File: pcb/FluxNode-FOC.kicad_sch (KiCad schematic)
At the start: 0 parts

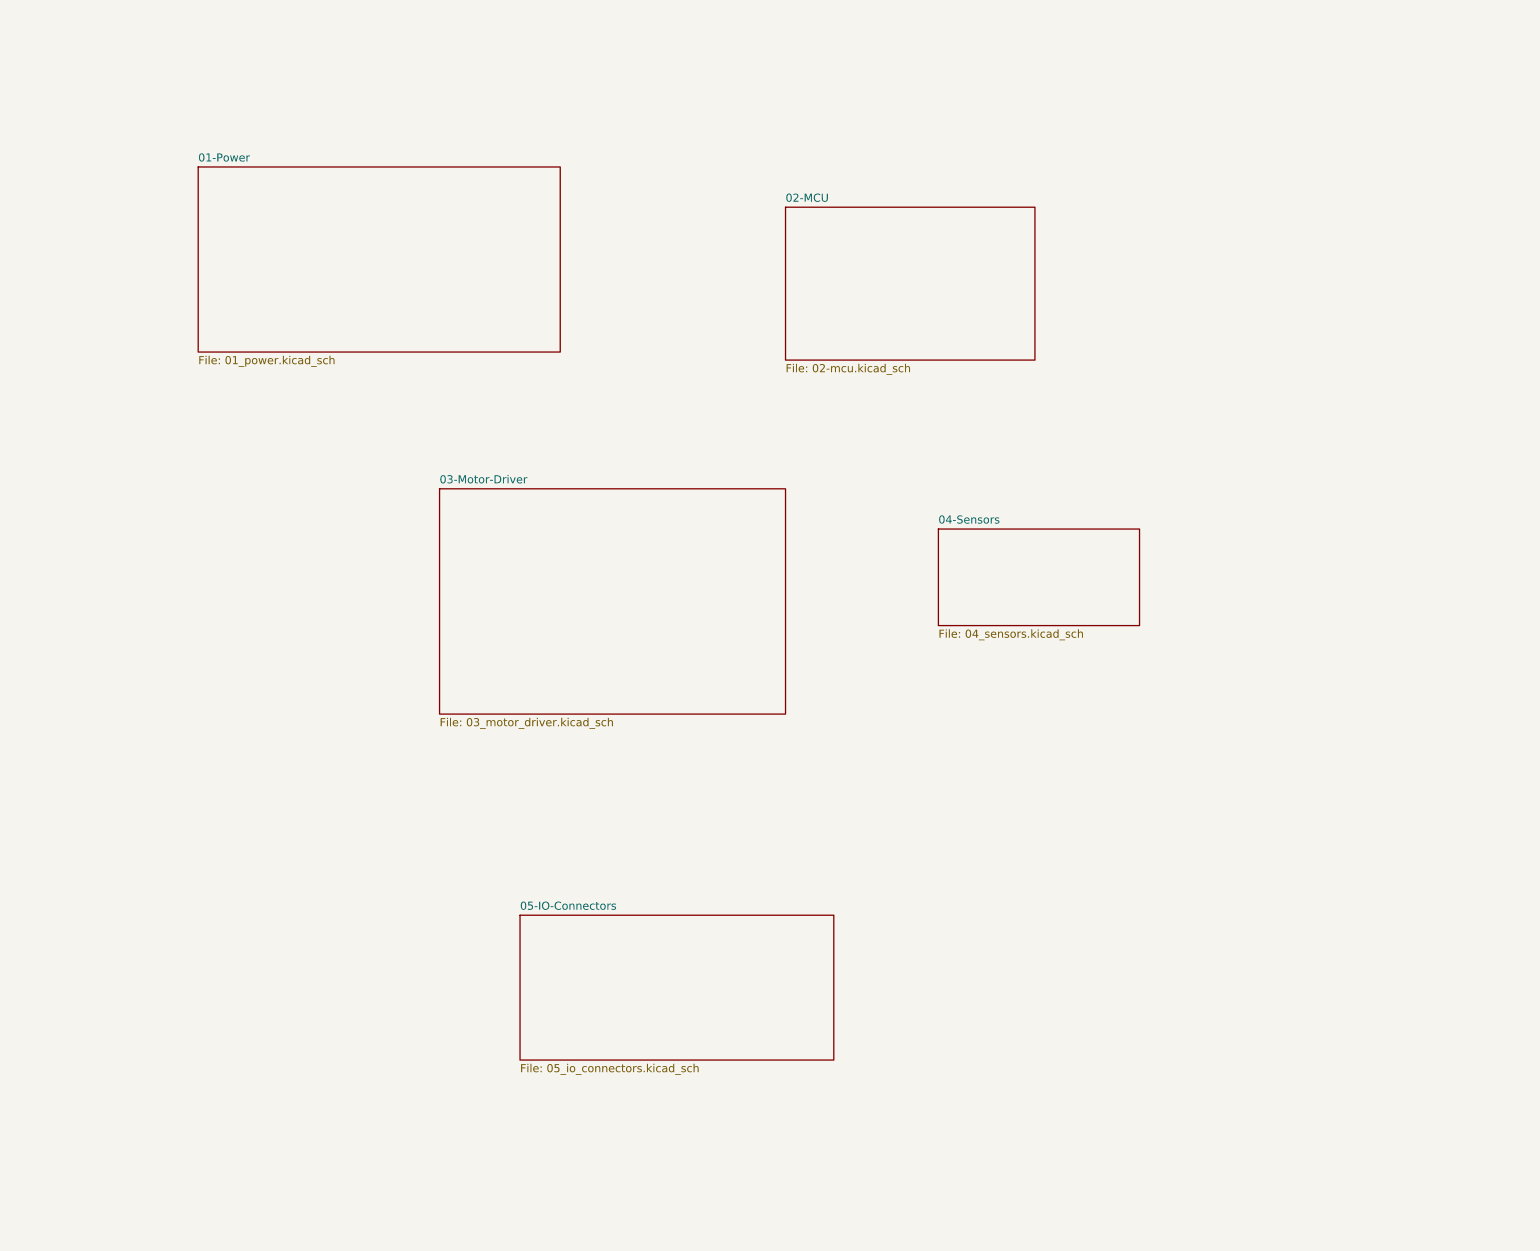
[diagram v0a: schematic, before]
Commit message: Setup project structure with organised sub-sheets
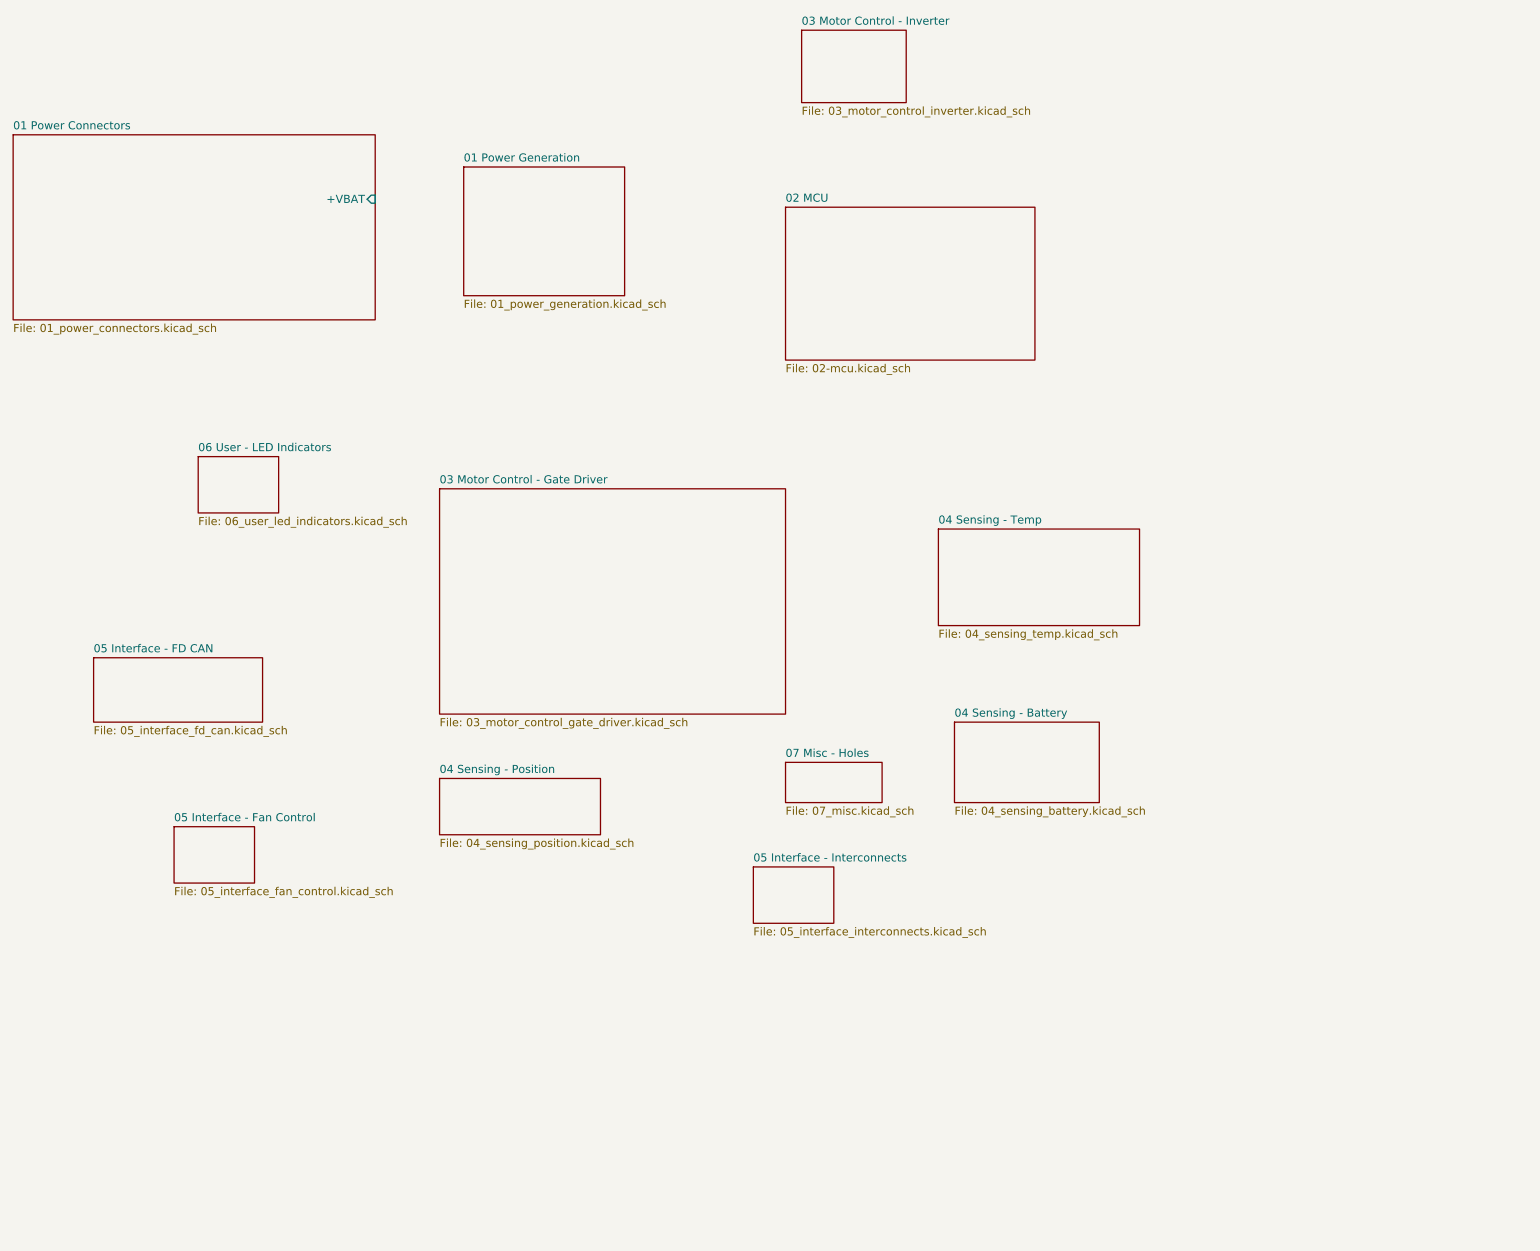
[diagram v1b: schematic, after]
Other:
- sheet 01-Power renamed 01 Power Connectors
- sheet 02-MCU renamed 02 MCU
- sheet 03-Motor-Driver renamed 03 Motor Control - Gate Driver
- sheet 04-Sensors renamed 04 Sensing - Temp
- removed sheet 05-IO-Connectors
- added sheet 01 Power Generation (01_power_generation.kicad_sch)
- added sheet 03 Motor Control - Inverter (03_motor_control_inverter.kicad_sch)
- added sheet 04 Sensing - Battery (04_sensing_battery.kicad_sch)
- added sheet 04 Sensing - Position (04_sensing_position.kicad_sch)
- added sheet 05 Interface - FD CAN (05_interface_fd_can.kicad_sch)
- added sheet 05 Interface - Fan Control (05_interface_fan_control.kicad_sch)
- added sheet 05 Interface - Interconnects (05_interface_interconnects.kicad_sch)
- added sheet 06 User - LED Indicators (06_user_led_indicators.kicad_sch)
- added sheet 07 Misc - Holes (07_misc.kicad_sch)
- sheet 01 Power Connectors: file 01_power.kicad_sch -> 01_power_connectors.kicad_sch
- sheet 01 Power Connectors ports: added +VBAT; removed none
- sheet 03 Motor Control - Gate Driver: file 03_motor_driver.kicad_sch -> 03_motor_control_gate_driver.kicad_sch
- sheet 04 Sensing - Temp: file 04_sensors.kicad_sch -> 04_sensing_temp.kicad_sch

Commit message: Created blockout and connections of all the major parts
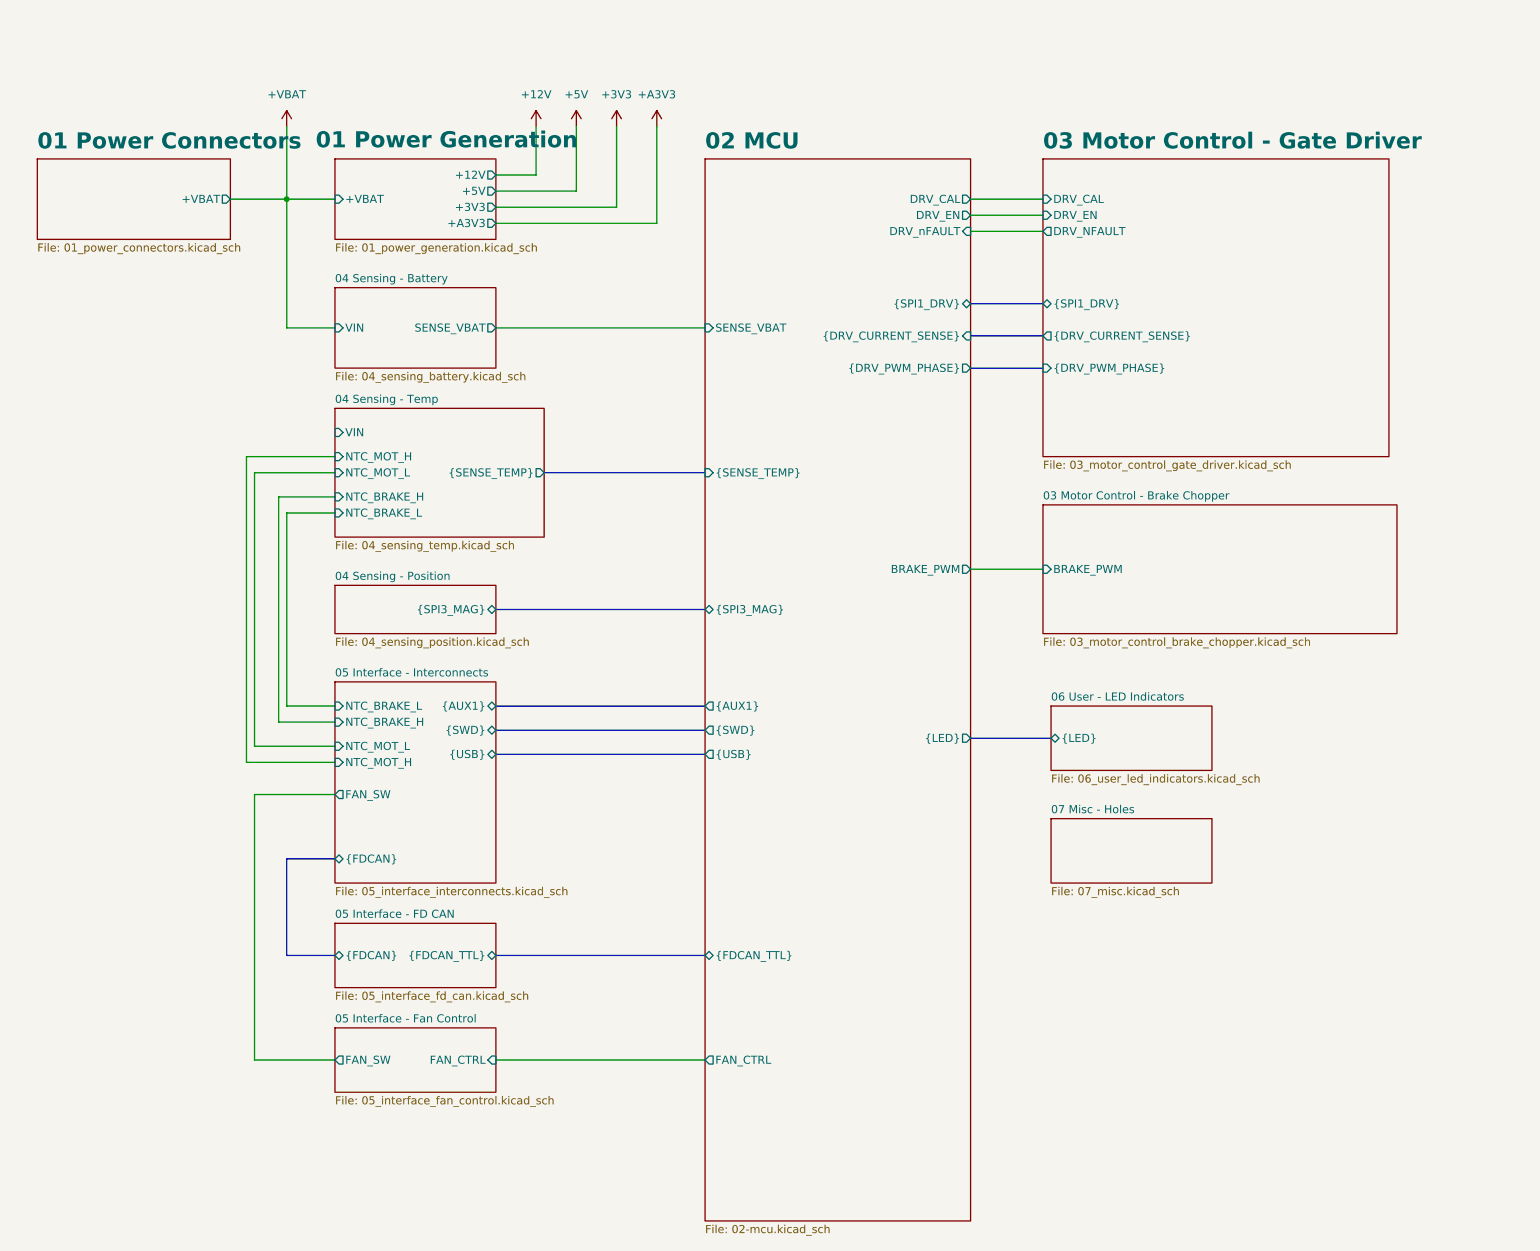
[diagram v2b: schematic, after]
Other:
- removed sheet 03 Motor Control - Inverter
- added sheet 03 Motor Control - Brake Chopper (03_motor_control_brake_chopper.kicad_sch)
- sheet 01 Power Generation ports: added +12V, +3V3, +5V, +A3V3, +VBAT; removed none
- sheet 02 MCU ports: added BRAKE_PWM, DRV_CAL, DRV_EN, DRV_nFAULT, FAN_CTRL, SENSE_VBAT, {AUX1}, {DRV_CURRENT_SENSE}, {DRV_PWM_PHASE}, {FDCAN_TTL}, {LED}, {SENSE_TEMP}, {SPI1_DRV}, {SPI3_MAG}, {SWD}, {USB}; removed none
- sheet 03 Motor Control - Gate Driver ports: added DRV_CAL, DRV_EN, DRV_NFAULT, {DRV_CURRENT_SENSE}, {DRV_PWM_PHASE}, {SPI1_DRV}; removed none
- sheet 04 Sensing - Battery ports: added SENSE_VBAT, VIN; removed none
- sheet 04 Sensing - Position ports: added {SPI3_MAG}; removed none
- sheet 04 Sensing - Temp ports: added NTC_BRAKE_H, NTC_BRAKE_L, NTC_MOT_H, NTC_MOT_L, VIN, {SENSE_TEMP}; removed none
- sheet 05 Interface - FD CAN ports: added {FDCAN_TTL}, {FDCAN}; removed none
- sheet 05 Interface - Fan Control ports: added FAN_CTRL, FAN_SW; removed none
- sheet 05 Interface - Interconnects ports: added FAN_SW, NTC_BRAKE_H, NTC_BRAKE_L, NTC_MOT_H, NTC_MOT_L, {AUX1}, {FDCAN}, {SWD}, {USB}; removed none
- sheet 06 User - LED Indicators ports: added {LED}; removed none

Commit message: Unified all different LCSC part numbers of the same exact components to just one variant
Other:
- sheet 02 MCU ports: added BRAKE_CTRL, {SENSE_PHASE_U}, {SPI1_MAG}; removed BRAKE_PWM, {SPI3_MAG}
- sheet 03 Motor Control - Brake Chopper ports: added BRAKE_CTRL, BRAKE_SW; removed BRAKE_PWM
- sheet 04 Sensing - Position ports: added {SPI1_MAG}; removed {SPI3_MAG}
- sheet 05 Interface - Interconnects ports: added BRAKE_SW; removed none
- company: (none) -> PhiMai
- title: (none) -> Project Blockout
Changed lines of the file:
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@@
 	(generator_version "10.0")
 	(paper "A3")
+	(title_block
+		(title "Project Blockout")
+		(date "2026-06-07")
+		(rev "0.1.0")
+		(company "PhiMai")
+	)
 	(junction
 		(at 64.77 46.99)
@@
 	(wire
 		(pts
+			(xy 58.42 140.97) (xy 72.39 140.97)
+		)
+		(stroke
+			(width 0)
+			(type default)
+		)
+	)
+	(wire
+		(pts
 			(xy 64.77 127) (xy 72.39 127)
 		)
@@
 	(wire
 		(pts
-			(xy 72.39 140.97) (xy 59.69 140.97)
+			(xy 72.39 146.05) (xy 59.69 146.05)
 		)
 		(stroke
@@
 		)
 	)
+	(wire
+		(pts
+			(xy 219.71 105.41) (xy 238.76 105.41)
+		)
+		(stroke
+			(width 0)
+			(type default)
+		)
+	)
 	(bus
 		(pts
@@
 	(wire
 		(pts
-			(xy 59.69 140.97) (xy 59.69 182.88)
+			(xy 59.69 146.05) (xy 59.69 182.88)
 		)
 		(stroke
@@
 			(width 0)
 			(type default)
+		)
+	)
+	(label "BRAKE_SW"
+		(at 238.76 105.41 180)
+		(effects
+			(font
+				(size 1.27 1.27)
+			)
+			(justify right bottom)
+		)
+	)
+	(label "BRAKE_SW"
+		(at 58.42 140.97 0)
+		(effects
+			(font
+				(size 1.27 1.27)
+			)
+			(justify left bottom)
 		)
 	)
@@
 			)
 		)
-		(pin "{SWD}" output
+		(pin "{SWD}" bidirectional
 			(at 130.81 130.81 180)
 			(effects
@@
 			)
 		)
-		(pin "BRAKE_PWM" output
+		(pin "{AUX1}" bidirectional
+			(at 130.81 127 180)
+			(effects
+				(font
+					(size 1.27 1.27)
+				)
+				(justify left)
+			)
+		)
+		(pin "{USB}" bidirectional
+			(at 130.81 134.62 180)
+			(effects
+				(font
+					(size 1.27 1.27)
+				)
+				(justify left)
+			)
+		)
+		(pin "BRAKE_CTRL" output
 			(at 172.72 105.41 0)
 			(effects
@@
 			)
 		)
-		(pin "{AUX1}" output
-			(at 130.81 127 180)
-			(effects
-				(font
-					(size 1.27 1.27)
-				)
-				(justify left)
-			)
-		)
-		(pin "{SPI3_MAG}" bidirectional
+		(pin "{SENSE_PHASE_U}" input
+			(at 172.72 78.74 0)
+			(effects
+				(font
+					(size 1.27 1.27)
+				)
+				(justify right)
+			)
+		)
+		(pin "{SPI1_MAG}" bidirectional
 			(at 130.81 111.76 180)
-			(effects
-				(font
-					(size 1.27 1.27)
-				)
-				(justify left)
-			)
-		)
-		(pin "{USB}" output
-			(at 130.81 134.62 180)
 			(effects
 				(font
@@
 			)
 		)
-		(pin "{SPI3_MAG}" bidirectional
+		(pin "{SPI1_MAG}" bidirectional
 			(at 97.79 111.76 0)
 			(effects
@@
 	(sheet
 		(at 184.15 95.25)
-		(size 55.88 20.32)
+		(size 35.56 20.32)
 		(exclude_from_sim no)
 		(in_bom yes)
@@
 			)
 		)
-		(pin "BRAKE_PWM" input
+		(pin "BRAKE_CTRL" input
 			(at 184.15 105.41 180)
 			(effects
@@
 				)
 				(justify left)
+			)
+		)
+		(pin "BRAKE_SW" output
+			(at 219.71 105.41 0)
+			(effects
+				(font
+					(size 1.27 1.27)
+				)
+				(justify right)
 			)
 		)
@@
 		)
 		(pin "FAN_SW" output
-			(at 72.39 140.97 180)
-			(effects
-				(font
-					(size 1.27 1.27)
-				)
-				(justify left)
-			)
-		)
-		(pin "NTC_BRAKE_H" input
+			(at 72.39 146.05 180)
+			(effects
+				(font
+					(size 1.27 1.27)
+				)
+				(justify left)
+			)
+		)
+		(pin "NTC_BRAKE_H" output
 			(at 72.39 129.54 180)
 			(effects
@@
 			)
 		)
-		(pin "NTC_BRAKE_L" input
+		(pin "NTC_BRAKE_L" output
 			(at 72.39 127 180)
 			(effects
@@
 				)
 				(justify right)
+			)
+		)
+		(pin "BRAKE_SW" input
+			(at 72.39 140.97 180)
+			(effects
+				(font
+					(size 1.27 1.27)
+				)
+				(justify left)
 			)
 		)
@@
 	)
 	(embedded_fonts no)
+	(embedded_files
+		(file
+			(name "FluxNode_sheet_template.kicad_wks")
+			(type worksheet)
+			(data |KLUv/WANCPUTAAaeXiEA1TZqxSYpSnAbOsWnapwROGKZeeGdkHc4TsT+/3+oZwJUAE0AWAD4I/F3
+				ODZP2tdysjdqfuNidVFrdudDK/JrxeqyaHvJlj/yJwAAARL0Xk5rUkpDZfw2dI1IUp3xe9mvcwiA
+				QIVRSg111r7YltlDBECg/Ig0oQfaDyH+31/TcNWeV6AijTJ4bb/npPfMfjMGX+zZk/qAWPzaxbff
+				3vkOLwhnr6n+6+OIwTqnVbt2eL3OeVm1doZlVjZpf/a+pKj20bsPeh7xf5itEvIKhlH9oNahs0kl
+				E66rbBgNQ1twD9Pgsi7r6klpZiE6gZ02i8bQbJeu40yDVvh7jJwzKftfB5u0sV+CPFdtqpHq1fP7
+				vkkNBMDFG9pX7RKTFKX6RwGBClERNctI1yNHvJg1I9Eokcki4bBoFMu2OToMM1iHiCbZIFzDNkAr
+				em+7ql0T1qQbxMJZxLeWSisNbb97pxMUToKQo/q9MeNNZyc9SmWjaJSS7UIRf32oXGygwUSoGJoS
+				SZIUMswBcESExuo2WZfljjON3a6gtMnTygZ+DlLtqI7d+jpbvWuDTDOiH9/KBOHNQdbWnxjDDGKg
+				8F6daGXWEq8l8oJXmqfyY5nCQxd7iiqYAERDAHcd161/VR6IdUtLFexiX7EiwA+KJgJmZc4HIOwx
+				WEqASxYsEnmfVWKnKwy47eFRT+mHoIkNeorOb4Xe8KCXmSk/ijdKyCKET4J/OkHzl5MOXhO44Yp9
+				Nu9NgNOyIWUeDXIFBK1mNsY4Dhf3Cq1oxHRvPMybMSpuptcLFNejLrBOMvb727uVFQttGATso8qd
+				3VG0vqyWrDUKe3hP/P+7HnEYH70K|
+			)
+			(checksum "13570387B61A404C098C5B87A1ED2AD9")
+		)
+	)
 )
